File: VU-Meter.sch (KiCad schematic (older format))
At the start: 17 parts, among them U6 U_LM3914N-1_NOPB

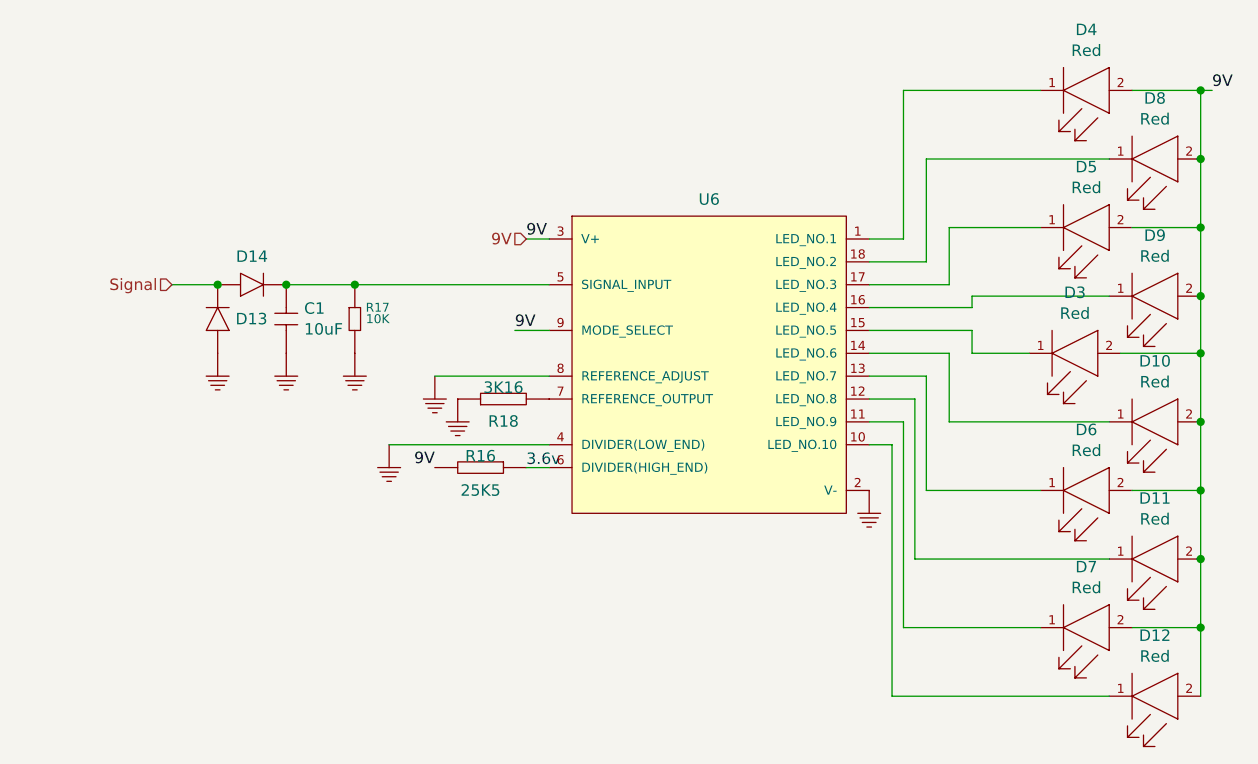
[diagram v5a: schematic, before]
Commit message: made schematic changed based on testing
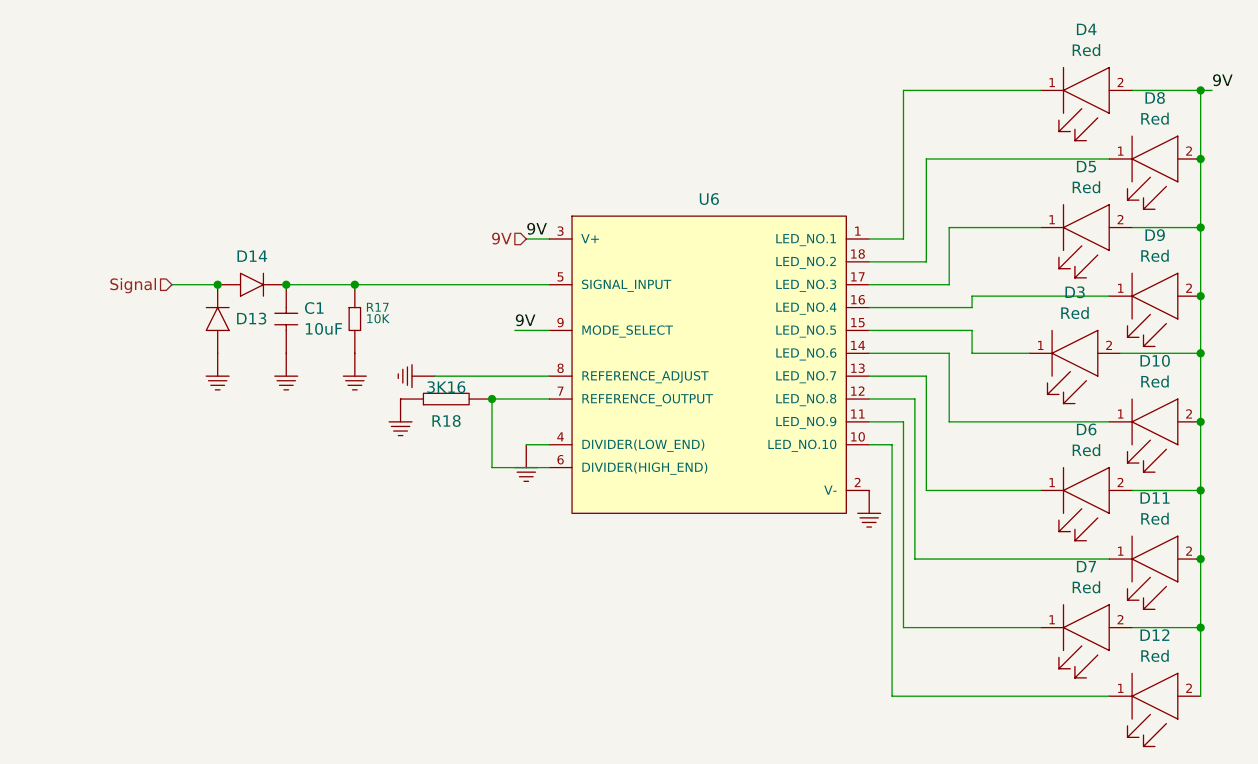
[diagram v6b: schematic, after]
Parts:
- removed R16: R_25K5_0603, MAIN_PCB_LIB:R_0603, symbol Main_Library:R_25K5_0603
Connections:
- net at U6.6 (DIVIDER(HIGH_END)): now also R18.2, U6.7 (REFERENCE_OUTPUT)
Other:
- note removed: "3.6v"
- moved on the sheet: R18
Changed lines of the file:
@@
 EESchema Schematic File Version 4
+LIBS:versterker-cache
 EELAYER 30 0
 EELAYER END
@@
 L Main_Library:R_3K16_0603 R18
 U 1 1 61702C03
-P 5650 4050
-F 0 "R18" V 5552 4050 50  0000 C CNN
-F 1 "R_3K16_0603" H 5650 4050 50  0001 C CNN
-F 2 "MAIN_PCB_LIB:R_0603" H 5650 4050 50  0001 C CNN
-F 3 "" H 5650 4050 50  0001 C CNN
-F 4 "603-RT0603BRD073K16L" H 5650 4050 50  0001 C CNN "mouser"
-F 5 "3K16" V 5700 4050 50  0000 C CNN "Waarde"
-	1    5650 4050
+P 5400 4050
+F 0 "R18" V 5302 4050 50  0000 C CNN
+F 1 "R_3K16_0603" H 5400 4050 50  0001 C CNN
+F 2 "MAIN_PCB_LIB:R_0603" H 5400 4050 50  0001 C CNN
+F 3 "" H 5400 4050 50  0001 C CNN
+F 4 "603-RT0603BRD073K16L" H 5400 4050 50  0001 C CNN "mouser"
+F 5 "3K16" V 5450 4050 50  0000 C CNN "Waarde"
+	1    5400 4050
 	0    -1   -1   0
 $EndComp
@@
 F 3 "" H 5260 3890 50  0001 C CNN
 	1    5350 3950
-	1    0    0    -1
+	0    1    1    0
 $EndComp
 $Comp
 L Main_Library:GND #GND023
 U 1 1 619C0A27
-P 5450 4050
-F 0 "#GND023" H 5290 4030 50  0001 C CNN
-F 1 "GND" H 5290 4030 50  0001 C CNN
-F 2 "" H 5360 3990 50  0001 C CNN
-F 3 "" H 5360 3990 50  0001 C CNN
-	1    5450 4050
-	1    0    0    -1
-$EndComp
-$Comp
-L Main_Library:R_25K5_0603 R16
-U 1 1 61B5A423
-P 5550 4350
-F 0 "R16" V 5500 4350 50  0000 C CNN
-F 1 "R_25K5_0603" H 5550 4800 50  0001 C CNN
-F 2 "MAIN_PCB_LIB:R_0603" H 5750 4870 50  0001 C CNN
-F 3 "" H 5500 4200 50  0001 C CNN
-F 4 "25K5" V 5650 4350 50  0000 C CNN "Waarde"
-F 5 "603-RT0603FRE0725K5L" H 5700 4950 50  0001 C CNN "Digi-Key"
-	1    5550 4350
-	0    1    1    0
-$EndComp
-Text Label 5350 4350 2    50   ~ 0
-9V
-Wire Wire Line
-	5750 4350 5850 4350
-Text Notes 5750 4350 0    50   ~ 0
-3.6v
+P 5200 4050
+F 0 "#GND023" H 5040 4030 50  0001 C CNN
+F 1 "GND" H 5040 4030 50  0001 C CNN
+F 2 "" H 5110 3990 50  0001 C CNN
+F 3 "" H 5110 3990 50  0001 C CNN
+	1    5200 4050
+	1    0    0    -1
+$EndComp
 Wire Wire Line
 	5750 3350 5850 3350
@@
 Connection ~ 5000 3550
 Wire Wire Line
-	5850 4250 5150 4250
-Wire Wire Line
 	5350 3950 5850 3950
 $Comp
 L Main_Library:GND #GND027
 U 1 1 61B320C3
-P 5150 4250
-F 0 "#GND027" H 4990 4230 50  0001 C CNN
-F 1 "GND" H 4990 4230 50  0001 C CNN
-F 2 "" H 5060 4190 50  0001 C CNN
-F 3 "" H 5060 4190 50  0001 C CNN
-	1    5150 4250
-	1    0    0    -1
-$EndComp
+P 5750 4250
+F 0 "#GND027" H 5590 4230 50  0001 C CNN
+F 1 "GND" H 5590 4230 50  0001 C CNN
+F 2 "" H 5660 4190 50  0001 C CNN
+F 3 "" H 5660 4190 50  0001 C CNN
+	1    5750 4250
+	1    0    0    -1
+$EndComp
+Wire Wire Line
+	5750 4250 5850 4250
+Wire Wire Line
+	5600 4050 5850 4050
+Wire Wire Line
+	5850 4350 5600 4350
+Wire Wire Line
+	5600 4350 5600 4050
+Connection ~ 5600 4050
 $EndSCHEMATC

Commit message: no message
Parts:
- added C9: C_1.5uF_0603_25V, MAIN_PCB_LIB:C_0603, symbol Main_Library:C_1.5uF_0603_25V
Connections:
- net Signal: now also C9.2; no longer D13.C, D14.A
- new net: C9.1, D13.C, D14.A
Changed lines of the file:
@@
 EESchema Schematic File Version 4
-LIBS:versterker-cache
 EELAYER 30 0
 EELAYER END
@@
 Text HLabel 5750 3350 0    50   Input ~ 0
 9V
-Text HLabel 4200 3550 0    50   Input ~ 0
+Text HLabel 3900 3550 0    50   Input ~ 0
 Signal
 $Comp
@@
 	5600 4350 5600 4050
 Connection ~ 5600 4050
+$Comp
+L Main_Library:C_1.5uF_0603_25V C?
+U 1 1 61B8FF25
+P 4050 3550
+AR Path="/6152C63E/61B8FF25" Ref="C?"  Part="1"
+AR Path="/616ED187/61B8FF25" Ref="C9"  Part="1"
+F 0 "C9" V 3859 3550 39  0000 C CNN
+F 1 "C_1.5uF_0603_25V" H 4050 3800 39  0001 C CNN
+F 2 "MAIN_PCB_LIB:C_0603" H 4100 3900 39  0001 C CNN
+F 3 "" H 3950 3600 39  0001 C CNN
+F 4 "1.5uF" V 3934 3550 39  0000 C CNN "Waarde"
+F 5 "445-5962-1-ND" H 4050 3850 39  0001 C CNN "Digi-Key"
+	1    4050 3550
+	0    1    1    0
+$EndComp
 $EndSCHEMATC

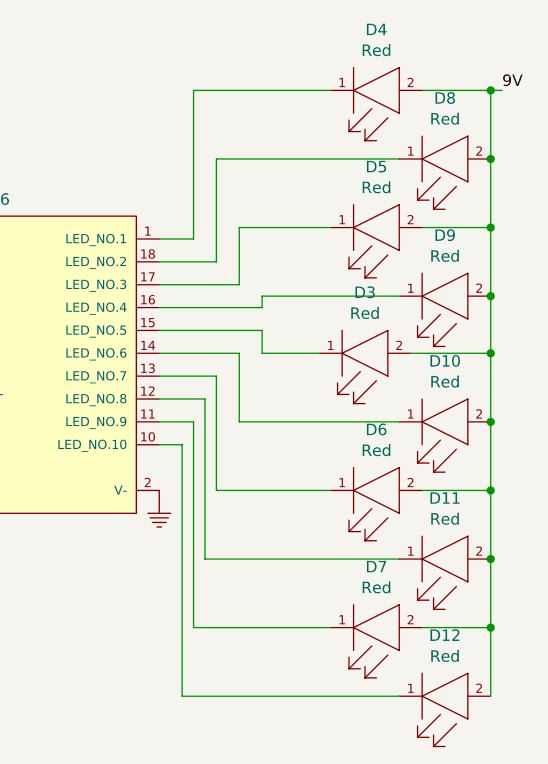
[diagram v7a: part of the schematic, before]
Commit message: changed partnumbers
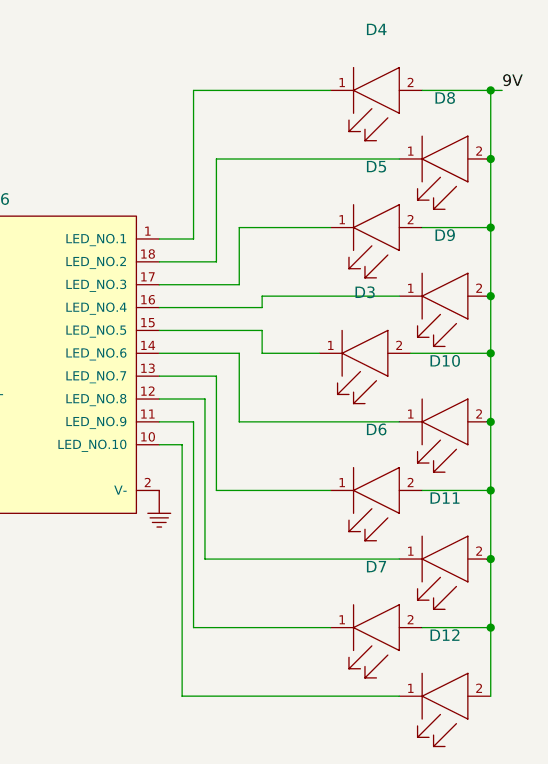
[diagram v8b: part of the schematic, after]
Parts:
- removed C1: C_10uF_0603, MAIN_PCB_LIB:C_0603, symbol Main_Library:C_10uF_0603
- added C1: C_10uF_0603_16V, MAIN_PCB_LIB:C_0603, symbol Main_Library:C_10uF_0603_16V
- C9: Digi-Key 445-5962-1-ND -> (none); Mouser (none) -> 810-C1608X5R1E155K
- D10, D11, D12, D3, D4, D5, D6, D7, D8, D9: Mouser (none) -> 710-150060RS75000; automotive No -> (none); category Diode -> (none); colour Red -> (none); device class L1 Optoelectronics -> (none); device class L2 LEDs -> (none); device class L3 unset -> (none); digikey description LED RED CLEAR 0603 SMD -> (none); digikey part number 732-4978-1-ND -> (none); forward current 20mA -> (none); forward voltage 2V -> (none); height 0.8mm -> (none); lead free Yes -> (none); led orientation Top View -> (none); library id cd4e03a66a96d806 -> (none); luminous intensity 250mcd -> (none); manufacturer Wurth -> (none); max junction temp +95°C -> (none); mouser description Standard LEDs - SMD WL-SMCW SMDMono TpVw Waterclr 0603 Red -> (none); mouser part number 710-150060RS75000 -> (none); package 0603 -> (none); peak emmision wavelength 630nm -> (none); power dissipation 72mW -> (none); reverse voltage 5V -> (none); rohs Yes -> (none); standoff height 0mm -> (none); temperature range high +85°C -> (none); temperature range low -40°C -> (none); viewing angle 140° -> (none); wavelength 625nm -> (none)
- R18: Mouser (none) -> 603-RT0603BRD073K16L; mouser 603-RT0603BRD073K16L -> (none)
- U6: Mouser (none) -> 926-LM3914N-1/NOPB; Voltage - Supply 3V ~ 20V -> (none); category IC -> (none); digikey description IC DRIVER DOT BAR DISPLAY 18-DIP -> (none); digikey part number LM3914N-1/NOPB-ND -> (none); ipc land pattern name DIP794W46P254L2286H533Q18 -> (none); lead free yes -> (none); library id d4e439a443ae1486 -> (none); manufacturer Texas Instruments -> (none); mouser part number 926-LM3914N-1/NOPB -> (none); package PDIP18 -> (none); rohs yes -> (none); temperature range high +70°C -> (none); temperature range low 0°C -> (none)
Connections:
- net at D14.C, R17.1, U6.5 (SIGNAL_INPUT): now also C1.1
